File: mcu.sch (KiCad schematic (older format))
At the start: 23 parts

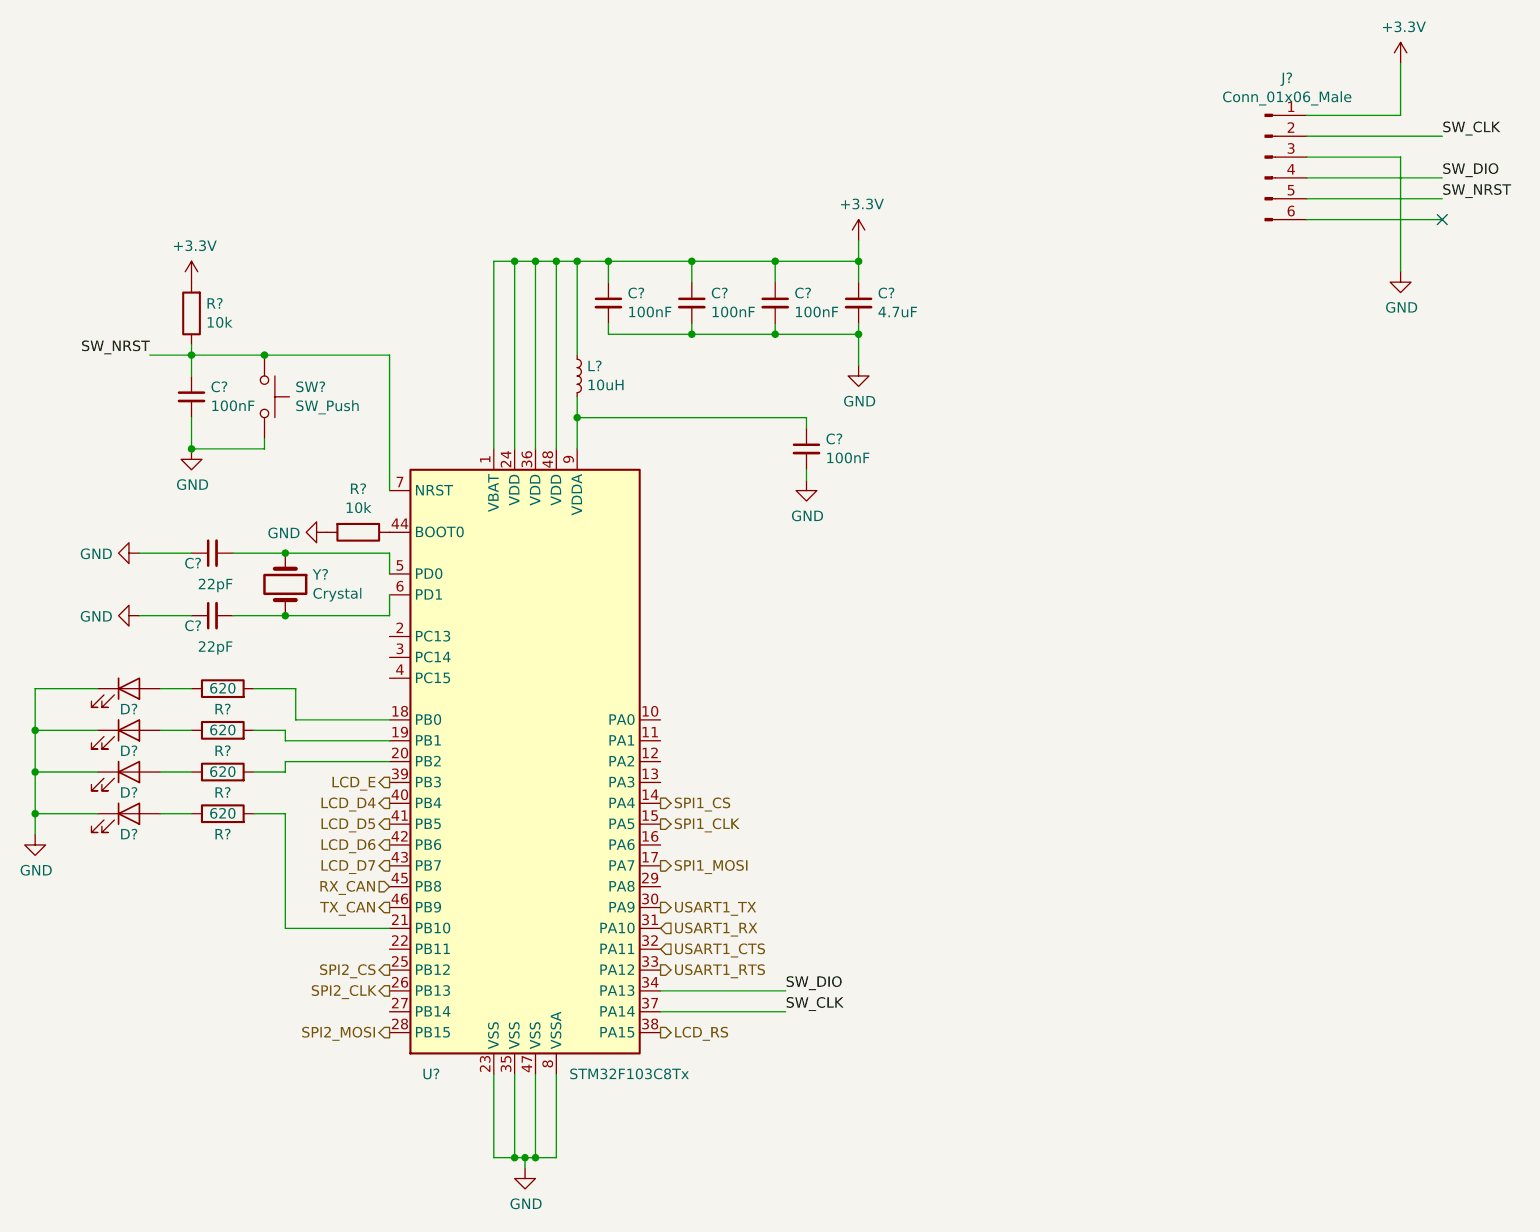
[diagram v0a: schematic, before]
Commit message: footprints; library for 7seg; start pcb layout
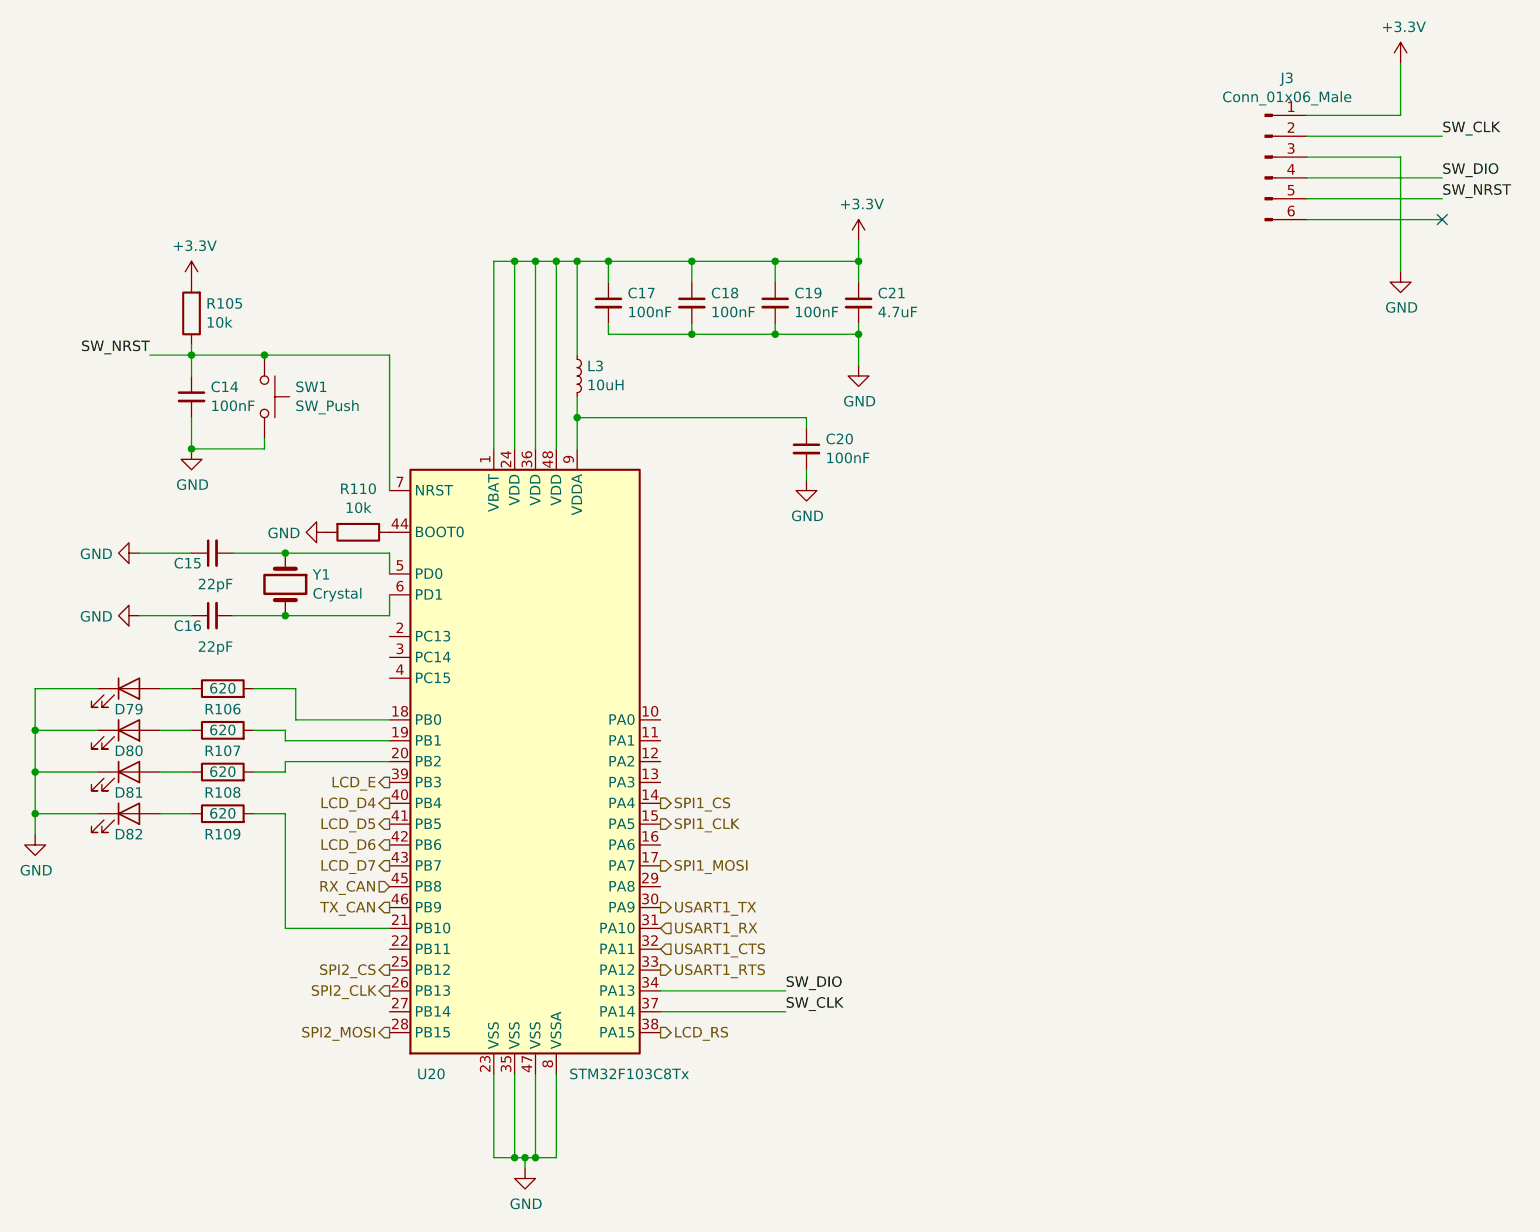
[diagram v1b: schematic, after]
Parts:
- C14, C15, C16, C17, C18, C19, C20, C21: renamed from C?; footprint (none) -> Capacitor_SMD:C_0603_1608Metric
- D79, D80, D81, D82: renamed from D?; footprint (none) -> LED_SMD:LED_0603_1608Metric
- J3: renamed from J?; footprint (none) -> Connector_PinHeader_2.54mm:PinHeader_1x06_P2.54mm_Vertical
- L3: renamed from L?; footprint (none) -> Inductor_SMD:L_0603_1608Metric
- R105, R106, R107, R108, R109, R110: renamed from R?; footprint (none) -> Resistor_SMD:R_0603_1608Metric
- SW1: renamed from SW?; footprint (none) -> Button_Switch_SMD:SW_Push_1P1T_NO_6x6mm_H9.5mm
- Y1: renamed from Y?; footprint (none) -> Crystal:Crystal_SMD_HC49-SD
- gave numbers to parts that had none: 1
